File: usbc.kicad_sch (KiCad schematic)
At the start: 4 parts, among them J1 USB_C_Plug_USB2.0_SMT, J4 Conn_01x04

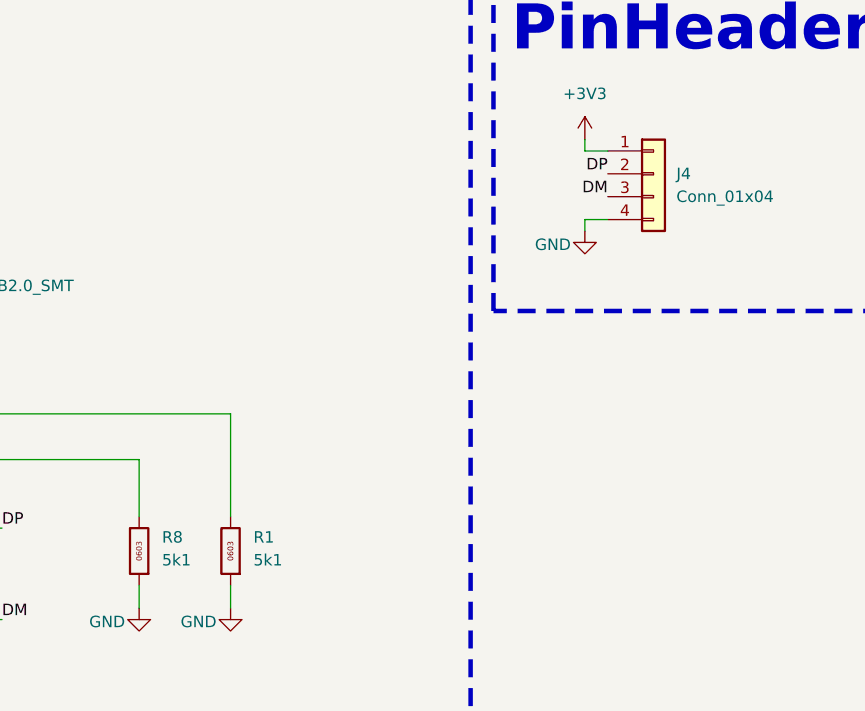
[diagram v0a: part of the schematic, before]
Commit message: fix: Buck Converter inductor changed to the right type
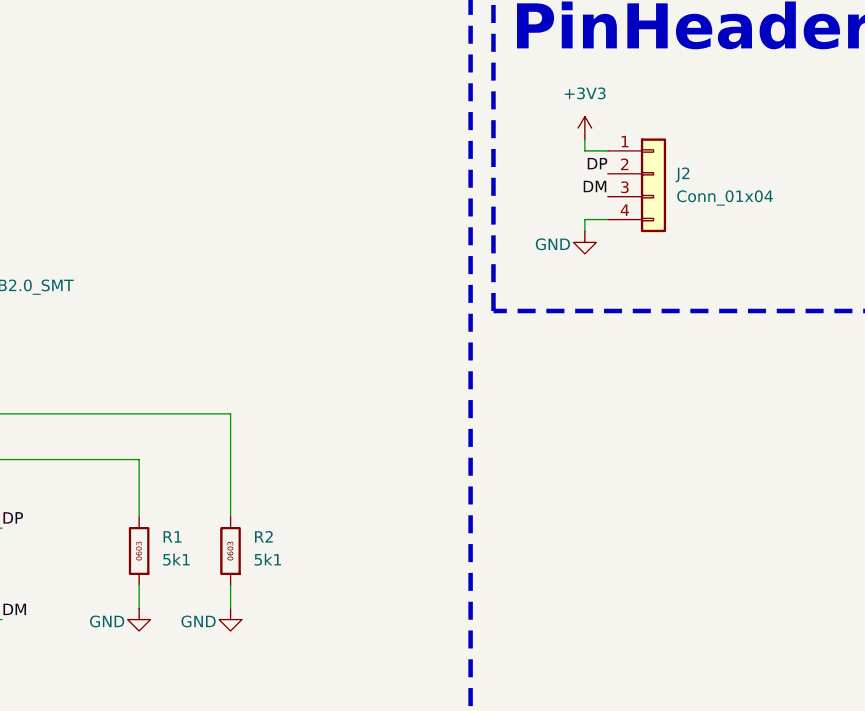
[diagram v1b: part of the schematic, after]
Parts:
- renumbered J4 to J2, R8 to R1, R1 to R2
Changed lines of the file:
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@@
 		(dnp no)
 		(fields_autoplaced yes)
-		(property "Reference" "#PWR010"
+		(property "Reference" "#PWR06"
 			(at 154.94 40.64 0)
 			(effects
@@
 			(project "projekt_Roland"
 				(path "/12081149-6dd0-47bb-bb21-fd1de250060f/3f61935e-2f8d-4290-af05-2d87358676e0"
-					(reference "#PWR010")
+					(reference "#PWR06")
 					(unit 1)
 				)
@@
 		(on_board yes)
 		(dnp no)
-		(property "Reference" "#PWR011"
+		(property "Reference" "#PWR07"
 			(at 154.94 53.34 0)
 			(effects
@@
 			(project "projekt_Roland"
 				(path "/12081149-6dd0-47bb-bb21-fd1de250060f/3f61935e-2f8d-4290-af05-2d87358676e0"
-					(reference "#PWR011")
+					(reference "#PWR07")
 					(unit 1)
 				)
@@
 		(on_board yes)
 		(dnp no)
-		(property "Reference" "R1"
+		(property "Reference" "R2"
 			(at 118.11 81.026 0)
 			(effects
@@
 			(project "projekt_Roland"
 				(path "/12081149-6dd0-47bb-bb21-fd1de250060f/3f61935e-2f8d-4290-af05-2d87358676e0"
-					(reference "R1")
+					(reference "R2")
 					(unit 1)
 				)
@@
 		(on_board yes)
 		(dnp no)
-		(property "Reference" "#PWR034"
+		(property "Reference" "#PWR04"
 			(at 105.41 95.25 0)
 			(effects
@@
 			(project "projekt_Roland"
 				(path "/12081149-6dd0-47bb-bb21-fd1de250060f/3f61935e-2f8d-4290-af05-2d87358676e0"
-					(reference "#PWR034")
+					(reference "#PWR04")
 					(unit 1)
 				)
@@
 		(on_board yes)
 		(dnp no)
-		(property "Reference" "R8"
+		(property "Reference" "R1"
 			(at 107.95 81.026 0)
 			(effects
@@
 			(project "projekt_Roland"
 				(path "/12081149-6dd0-47bb-bb21-fd1de250060f/3f61935e-2f8d-4290-af05-2d87358676e0"
-					(reference "R8")
+					(reference "R1")
 					(unit 1)
 				)
@@
 		(dnp no)
 		(fields_autoplaced yes)
-		(property "Reference" "J4"
+		(property "Reference" "J2"
 			(at 165.1 40.6399 0)
 			(effects
@@
 			(project ""
 				(path "/12081149-6dd0-47bb-bb21-fd1de250060f/3f61935e-2f8d-4290-af05-2d87358676e0"
-					(reference "J4")
+					(reference "J2")
 					(unit 1)
 				)
@@
 		(on_board yes)
 		(dnp no)
-		(property "Reference" "#PWR035"
+		(property "Reference" "#PWR05"
 			(at 115.57 95.25 0)
 			(effects
@@
 			(project "projekt_Roland"
 				(path "/12081149-6dd0-47bb-bb21-fd1de250060f/3f61935e-2f8d-4290-af05-2d87358676e0"
-					(reference "#PWR035")
-					(unit 1)
-				)
+					(reference "#PWR05")
+					(unit 1)
+				)
